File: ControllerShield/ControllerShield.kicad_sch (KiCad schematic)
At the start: 26 parts, among them J1 Power, J2 Digital/PWM, J3 Analog, J4 Digital/PWM, J5 Conn_02x05_Odd_Even, J6 Debug Point, SW1 Small Switch TH, U1 COM-09032, U2 LIS3DHTR, U3 TLV75533PDBV, U4 PCA9306DQER

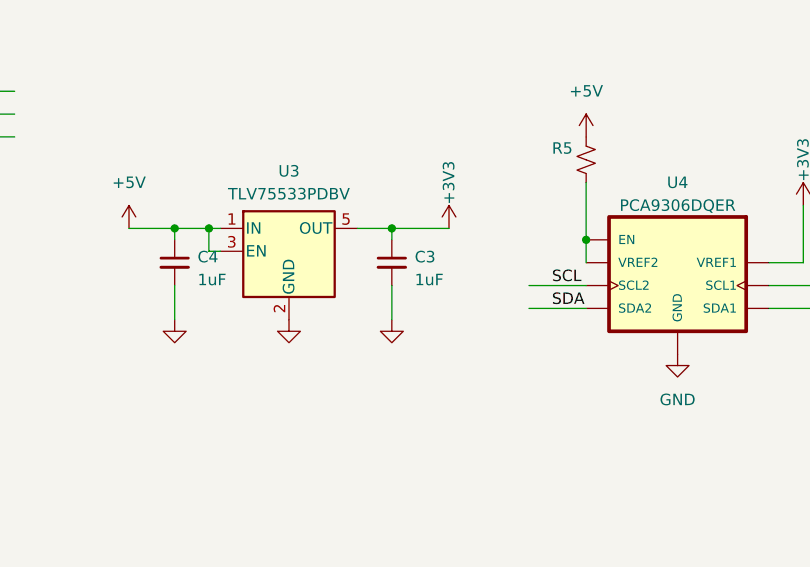
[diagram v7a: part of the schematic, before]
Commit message: Change footprint for level shifter to something more reasonable.
Add lots of cap to controller.

Add level shifter to controller
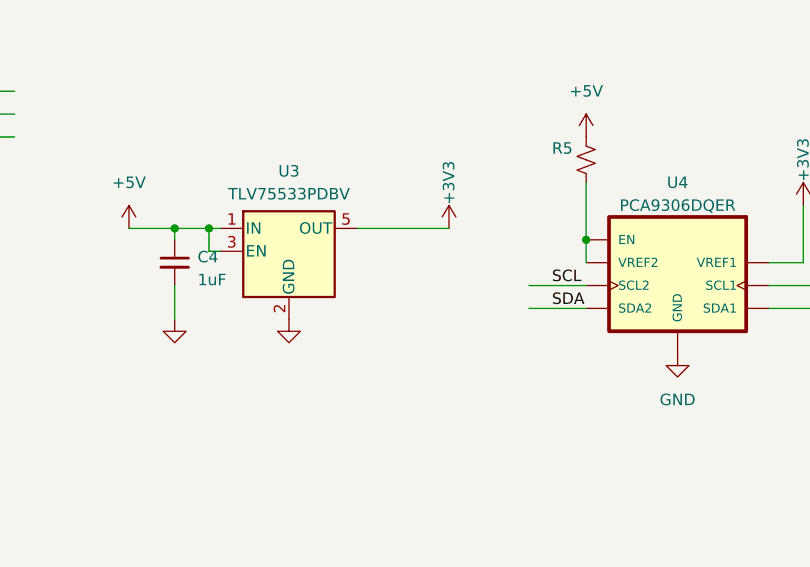
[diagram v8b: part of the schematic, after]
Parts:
- removed C3: 1uF, Capacitor_SMD:C_0603_1608Metric, symbol Device:C_Small
- U4: footprint TexasInstruments:SON35P140X100X40-8N -> Package_SO:TSSOP-8_3x3mm_P0.65mm
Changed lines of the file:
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@@
   (junction (at 124.46 116.84) (diameter 0) (color 0 0 0 0)
-  )
-  (junction (at 148.59 116.84) (diameter 0) (color 0 0 0 0)
   )
   (junction (at 31.75 46.99) (diameter 1.016) (color 0 0 0 0)
@@
     (stroke (width 0) (type default))
   )
-  (wire (pts (xy 148.59 123.19) (xy 148.59 127))
-    (stroke (width 0) (type default))
-  )
   (wire (pts (xy 63.5 148.59) (xy 63.5 138.43))
     (stroke (width 0) (type default))
@@
     (stroke (width 0) (type default))
   )
-  (wire (pts (xy 148.59 116.84) (xy 154.94 116.84))
-    (stroke (width 0) (type default))
-  )
   (wire (pts (xy 168.91 57.15) (xy 180.34 57.15))
     (stroke (width 0) (type default))
@@
     (stroke (width 0) (type default))
   )
-  (wire (pts (xy 148.59 116.84) (xy 148.59 118.11))
-    (stroke (width 0) (type default))
-  )
   (wire (pts (xy 180.34 41.91) (xy 177.8 41.91))
     (stroke (width 0) (type default))
@@
     (stroke (width 0) (type default))
   )
-  (wire (pts (xy 144.78 116.84) (xy 148.59 116.84))
+  (wire (pts (xy 144.78 116.84) (xy 154.94 116.84))
     (stroke (width 0) (type default))
   )
@@
     )
   )
-  (symbol (lib_id "Device:C_Small") (at 148.59 120.65 0) (unit 1)
-    (in_bom yes) (on_board yes) (dnp no) (fields_autoplaced)
-    (property "Reference" "C3" (at 151.13 120.0213 0)
-      (effects (font (size 1.27 1.27)) (justify left))
-    )
-    (property "Value" "1uF" (at 151.13 122.5613 0)
-      (effects (font (size 1.27 1.27)) (justify left))
-    )
-    (property "Footprint" "Capacitor_SMD:C_0603_1608Metric" (at 148.59 120.65 0)
-      (effects (font (size 1.27 1.27)) hide)
-    )
-    (property "Datasheet" "~" (at 148.59 120.65 0)
-      (effects (font (size 1.27 1.27)) hide)
-    )
-    (pin "1")
-    (pin "2")
-    (instances
-      (project "ControllerShield"
-        (path "/e63e39d7-6ac0-4ffd-8aa3-1841a4541b55"
-          (reference "C3") (unit 1)
-        )
-      )
-    )
-  )
   (symbol (lib_id "Device:R_Small_US") (at 209.55 109.22 0) (unit 1)
     (in_bom yes) (on_board yes) (dnp no)
@@
       (effects (font (size 1.27 1.27)))
     )
-    (property "Footprint" "TexasInstruments:SON35P140X100X40-8N" (at 175.26 120.65 0)
+    (property "Footprint" "Package_SO:TSSOP-8_3x3mm_P0.65mm" (at 175.26 120.65 0)
       (effects (font (size 1.27 1.27)) (justify bottom) hide)
     )
@@
         )
       )
-    )
-  )
-  (symbol (lib_id "power:GND") (at 148.59 127 0) (unit 1)
-    (in_bom yes) (on_board yes) (dnp no) (fields_autoplaced)
-    (property "Reference" "#PWR026" (at 148.59 133.35 0)
-      (effects (font (size 1.27 1.27)) hide)
-    )
-    (property "Value" "GND" (at 148.59 132.08 0)
-      (effects (font (size 1.27 1.27)) hide)
-    )
-    (property "Footprint" "" (at 148.59 127 0)
-      (effects (font (size 1.27 1.27)) hide)
-    )
-    (property "Datasheet" "" (at 148.59 127 0)
-      (effects (font (size 1.27 1.27)) hide)
-    )
-    (pin "1")
-    (instances
-      (project "ControllerShield"
-        (path "/e63e39d7-6ac0-4ffd-8aa3-1841a4541b55"
-          (reference "#PWR026") (unit 1)
-        )
-      )
